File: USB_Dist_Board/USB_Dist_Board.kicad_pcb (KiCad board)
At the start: 2 copper layers, 73 x 64.5 mm, 60 parts, among them P1 CONN_02X06, P2 CONN_01X03, P3 CONN_01X03, P5 CONN_01X04, P6 CONN_01X04, P7 CONN_02X06, Q1 BSS84, Q3 BSS84, SW1 RESET, SW2 BOOT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

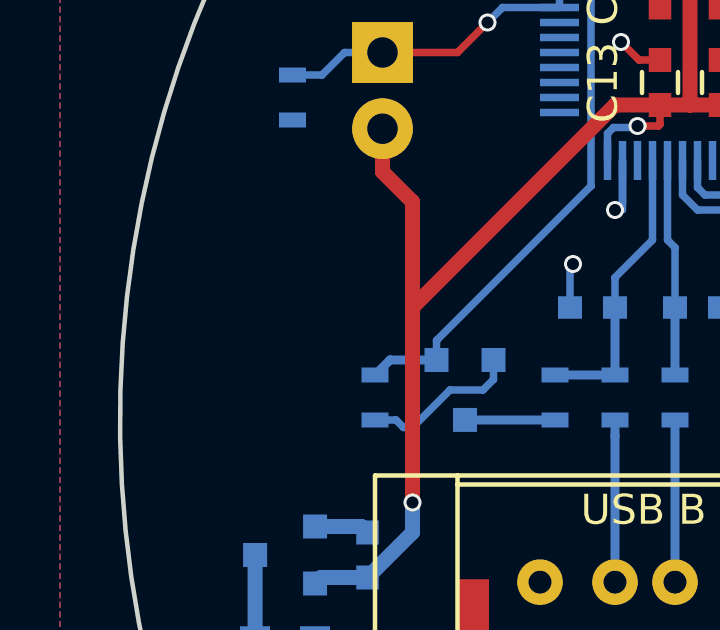
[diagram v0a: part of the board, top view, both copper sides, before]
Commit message: Resize PCBs
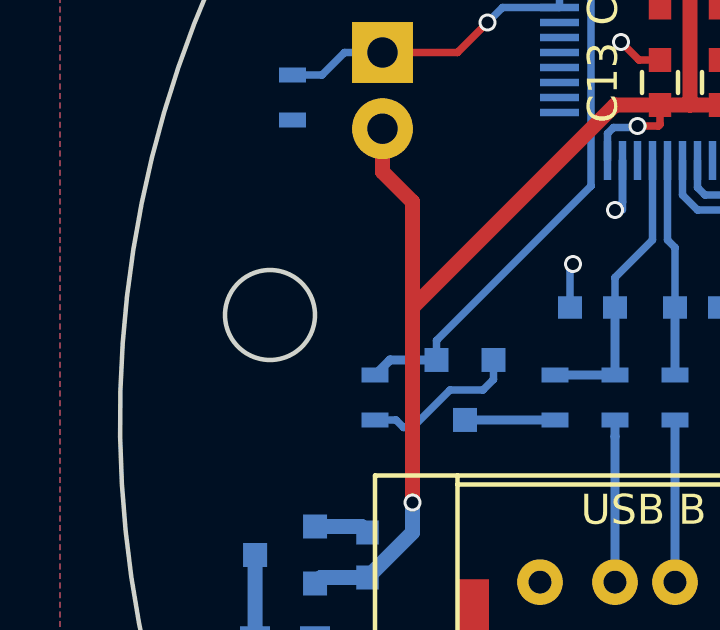
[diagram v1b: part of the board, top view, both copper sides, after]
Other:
- outline, holes or cut-outs redrawn
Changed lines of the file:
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@@
     (area 63.425047 63.425047 136.574953 128.035601)
     (thickness 1.6)
-    (drawings 10)
+    (drawings 11)
     (tracks 451)
     (zones 0)
@@
     )
   )
+  (gr_circle (center 68.5 96.5) (end 68.5 98) (layer Edge.Cuts) (width 0.15))
   (gr_line (start 76.53825 127.9606) (end 123.4617 127.9606) (layer Edge.Cuts) (width 0.15))
   (gr_arc (start 100 100) (end 123.4617 127.9606) (angle -280) (layer Edge.Cuts) (width 0.15))

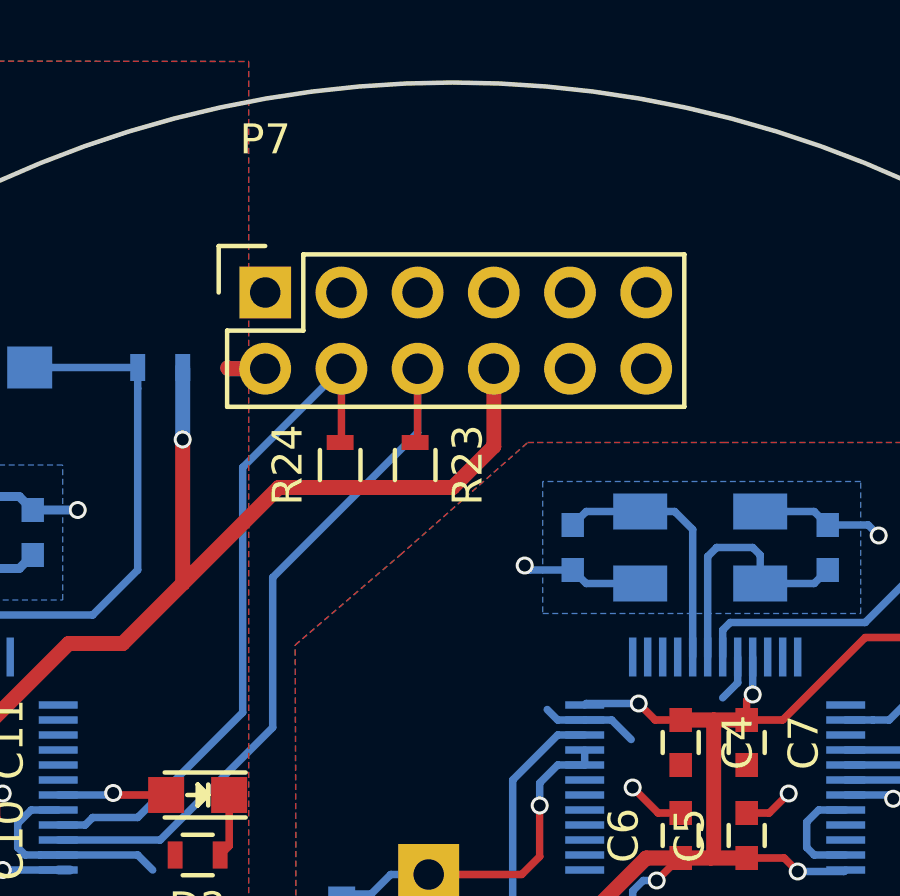
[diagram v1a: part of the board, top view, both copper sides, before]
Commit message: Add Power Distribution Board
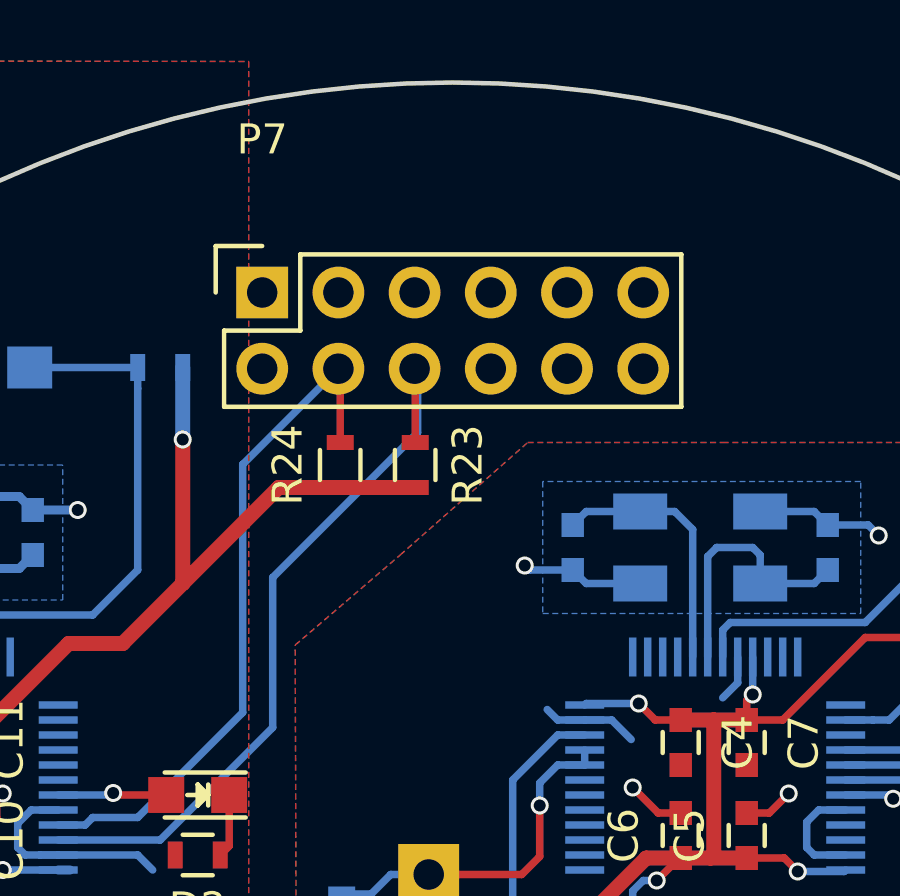
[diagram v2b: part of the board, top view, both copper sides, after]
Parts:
- moved P7 0.10 mm to (93.7, 70.5)
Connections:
- P7 pad 2: /USB_B_GND -> (no net)
- P7 pad 8: /3V3_B -> (no net)
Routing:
- net /3V3_B: track 90.0 -> 84.2 mm
- net /USB_B_GND: track 33.3 -> 30.8 mm
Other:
- net class Default: trace_width 0.25 -> 0.5
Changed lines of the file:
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@@
 (kicad_pcb (version 4) (host pcbnew 4.0.4-stable)
   (general
-    (links 161)
+    (links 159)
     (no_connects 0)
     (area 63.425047 63.425047 136.574953 128.035601)
     (thickness 1.6)
     (drawings 11)
-    (tracks 451)
+    (tracks 445)
     (zones 0)
     (modules 60)
@@
   )
   (setup
-    (last_trace_width 0.25)
+    (last_trace_width 0.5)
     (trace_clearance 0.2)
     (zone_clearance 0.508)
@@
   (net_class Default "This is the default net class."
     (clearance 0.2)
-    (trace_width 0.25)
+    (trace_width 0.5)
     (via_dia 0.6)
     (via_drill 0.4)
@@
   )
   (module Socket_Strips:Socket_Strip_Straight_2x06 (layer F.Cu)
-    (at 93.75 70.5)
+    (at 93.65 70.5)
     (descr "Through hole socket strip")
     (tags "socket strip")
@@
     (fp_line (start -1.55 -1.55) (end -1.55 0) (layer F.SilkS) (width 0.15))
     (pad 1 thru_hole rect (at 0 0) (size 1.7272 1.7272) (drill 1.016) (layers *.Cu *.Mask F.SilkS))
-    (pad 2 thru_hole oval (at 0 2.54) (size 1.7272 1.7272) (drill 1.016) (layers *.Cu *.Mask F.SilkS)
-      (net 50 /USB_B_GND))
+    (pad 2 thru_hole oval (at 0 2.54) (size 1.7272 1.7272) (drill 1.016) (layers *.Cu *.Mask F.SilkS))
     (pad 3 thru_hole oval (at 2.54 0) (size 1.7272 1.7272) (drill 1.016) (layers *.Cu *.Mask F.SilkS))
     (pad 4 thru_hole oval (at 2.54 2.54) (size 1.7272 1.7272) (drill 1.016) (layers *.Cu *.Mask F.SilkS)
@@
       (net 41 /SDA))
     (pad 7 thru_hole oval (at 7.62 0) (size 1.7272 1.7272) (drill 1.016) (layers *.Cu *.Mask F.SilkS))
-    (pad 8 thru_hole oval (at 7.62 2.54) (size 1.7272 1.7272) (drill 1.016) (layers *.Cu *.Mask F.SilkS)
-      (net 39 /3V3_B))
+    (pad 8 thru_hole oval (at 7.62 2.54) (size 1.7272 1.7272) (drill 1.016) (layers *.Cu *.Mask F.SilkS))
     (pad 9 thru_hole oval (at 10.16 0) (size 1.7272 1.7272) (drill 1.016) (layers *.Cu *.Mask F.SilkS))
     (pad 10 thru_hole oval (at 10.16 2.54) (size 1.7272 1.7272) (drill 1.016) (layers *.Cu *.Mask F.SilkS))
@@
   (segment (start 94.2 77) (end 91 80.2) (width 0.5) (layer F.Cu) (net 39))
   (segment (start 98.75 77) (end 96.25 77) (width 0.5) (layer F.Cu) (net 39))
-  (segment (start 101.37 75.63) (end 100 77) (width 0.5) (layer F.Cu) (net 39))
-  (segment (start 100 77) (end 98.75 77) (width 0.5) (layer F.Cu) (net 39))
-  (segment (start 101.37 73.04) (end 101.37 75.63) (width 0.5) (layer F.Cu) (net 39))
   (segment (start 72 100) (end 72.7 100) (width 0.25) (layer B.Cu) (net 39))
   (segment (start 72.7 100) (end 72.95 100.25) (width 0.25) (layer B.Cu) (net 39))
@@
   (via (at 79.75 84.25) (size 0.6) (drill 0.4) (layers F.Cu B.Cu) (net 39))
   (segment (start 86.85 89.75) (end 87.25 89.75) (width 0.3) (layer B.Cu) (net 39))
-  (segment (start 93 84.5) (end 93 76.33) (width 0.25) (layer B.Cu) (net 40))
-  (segment (start 93 76.33) (end 96.29 73.04) (width 0.25) (layer B.Cu) (net 40))
-  (segment (start 89.5 88) (end 93 84.5) (width 0.25) (layer B.Cu) (net 40))
-  (segment (start 88 88) (end 89.5 88) (width 0.25) (layer B.Cu) (net 40))
+  (segment (start 96.25 75.5) (end 96.25 73.1) (width 0.25) (layer F.Cu) (net 40))
+  (segment (start 96.25 73.1) (end 96.19 73.04) (width 0.25) (layer F.Cu) (net 40))
   (segment (start 86.85 88.25) (end 87.75 88.25) (width 0.25) (layer B.Cu) (net 40))
   (segment (start 87.75 88.25) (end 88 88) (width 0.25) (layer B.Cu) (net 40))
-  (segment (start 96.29 73.04) (end 96.29 75.46) (width 0.25) (layer F.Cu) (net 40))
+  (segment (start 88 88) (end 89.5 88) (width 0.25) (layer B.Cu) (net 40))
+  (segment (start 89.5 88) (end 93 84.5) (width 0.25) (layer B.Cu) (net 40))
+  (segment (start 93 84.5) (end 93 76.23) (width 0.25) (layer B.Cu) (net 40))
+  (segment (start 93 76.23) (end 96.19 73.04) (width 0.25) (layer B.Cu) (net 40))
   (segment (start 96.29 75.46) (end 96.25 75.5) (width 0.25) (layer F.Cu) (net 40))
+  (segment (start 98.75 75.5) (end 98.75 73.06) (width 0.25) (layer F.Cu) (net 41))
+  (segment (start 98.75 73.06) (end 98.73 73.04) (width 0.25) (layer F.Cu) (net 41))
   (segment (start 86.85 88.75) (end 90.25 88.75) (width 0.25) (layer B.Cu) (net 41))
   (segment (start 90.25 88.75) (end 94 85) (width 0.25) (layer B.Cu) (net 41))
@@
   (segment (start 94 80) (end 98.83 75.17) (width 0.25) (layer B.Cu) (net 41))
   (segment (start 98.83 75.17) (end 98.83 73.04) (width 0.25) (layer B.Cu) (net 41))
-  (segment (start 98.83 73.04) (end 98.83 75.42) (width 0.25) (layer F.Cu) (net 41))
-  (segment (start 98.83 75.42) (end 98.75 75.5) (width 0.25) (layer F.Cu) (net 41))
   (segment (start 83.8 78.5) (end 84 78.7) (width 0.25) (layer B.Cu) (net 42))
   (segment (start 84 78.7) (end 84 79.7) (width 0.25) (layer B.Cu) (net 42))
@@
   (segment (start 78.1 73) (end 80 73) (width 0.25) (layer B.Cu) (net 50))
   (via (at 80 73) (size 0.6) (drill 0.4) (layers F.Cu B.Cu) (net 50))
-  (segment (start 93.75 73.04) (end 92.528686 73.04) (width 0.5) (layer B.Cu) (net 50))
-  (segment (start 92.528686 73.04) (end 92.5 73.011314) (width 0.5) (layer B.Cu) (net 50))
-  (segment (start 93.75 73.04) (end 92.528686 73.04) (width 0.5) (layer F.Cu) (net 50))
-  (segment (start 92.528686 73.04) (end 92.5 73.011314) (width 0.5) (layer F.Cu) (net 50))
   (segment (start 80.25 91.35) (end 80.25 92.75) (width 0.25) (layer B.Cu) (net 50))
   (segment (start 80.25 92.75) (end 80 93) (width 0.25) (layer B.Cu) (net 50))

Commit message: Commit update
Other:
- outline, holes or cut-outs redrawn
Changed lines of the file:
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@@
     (links 159)
     (no_connects 0)
-    (area 63.425047 63.425047 136.574953 128.035601)
+    (area 61.5 62.75 141.000001 128.035601)
     (thickness 1.6)
     (drawings 11)
@@
     )
   )
-  (gr_circle (center 68.5 96.5) (end 68.5 98) (layer Edge.Cuts) (width 0.15))
+  (gr_circle (center 67 96.5) (end 67 98) (layer Edge.Cuts) (width 0.15))
   (gr_line (start 76.53825 127.9606) (end 123.4617 127.9606) (layer Edge.Cuts) (width 0.15))
   (gr_arc (start 100 100) (end 123.4617 127.9606) (angle -280) (layer Edge.Cuts) (width 0.15))

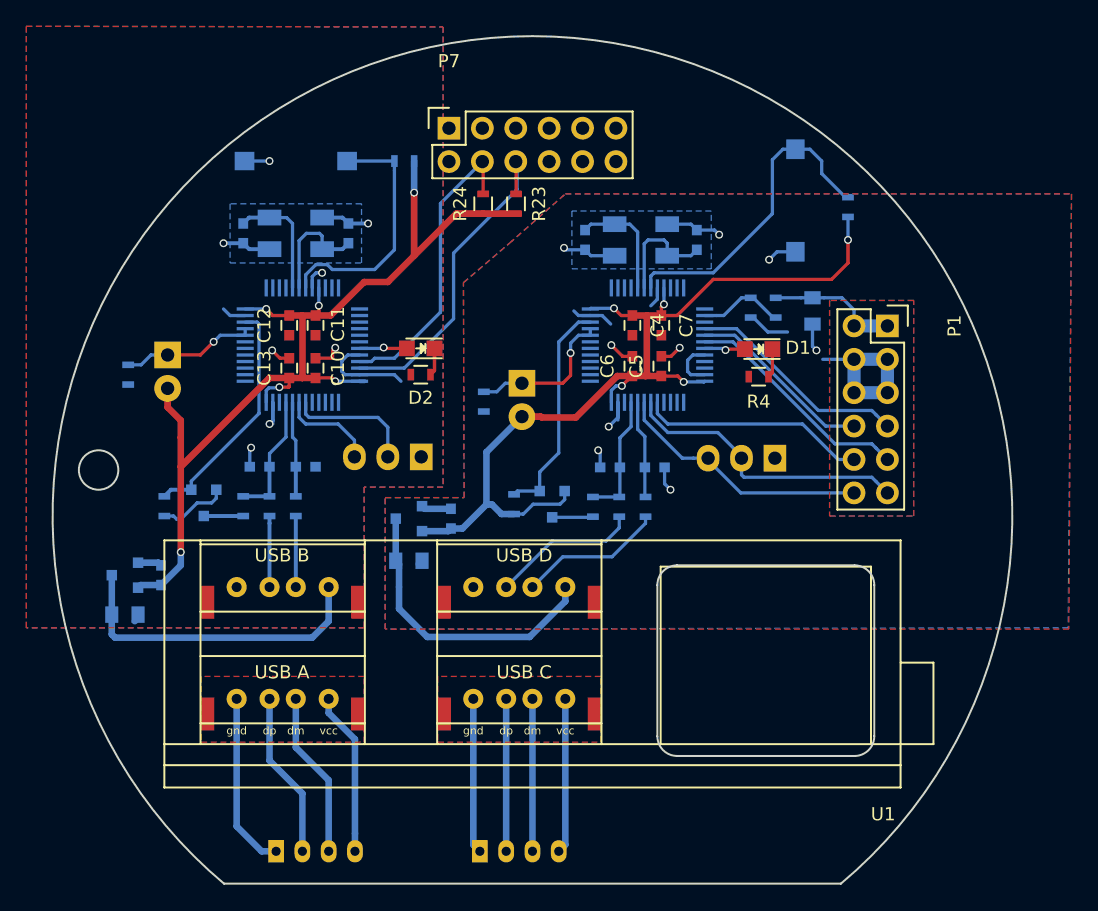
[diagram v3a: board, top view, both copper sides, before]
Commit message: USB_Dist_Board change pin map
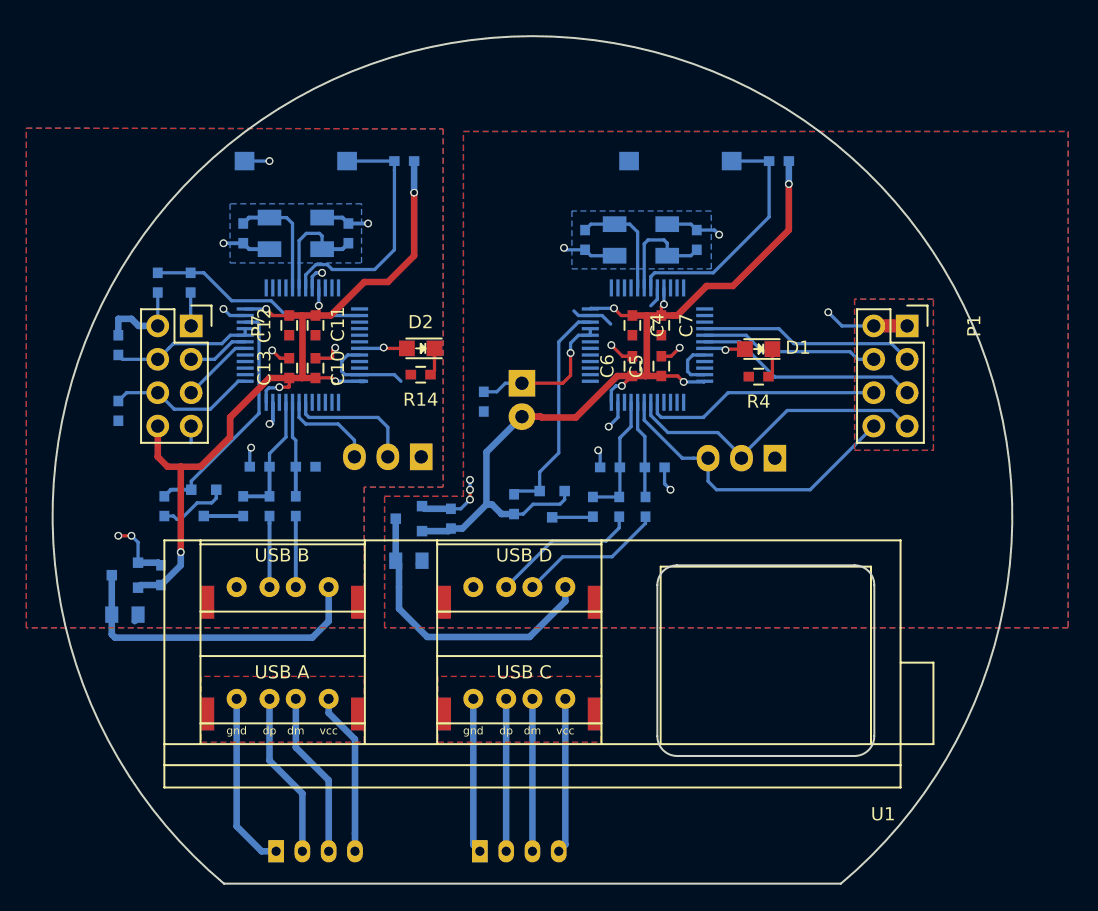
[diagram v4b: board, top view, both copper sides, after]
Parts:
- removed C1: C, Capacitors_SMD:C_0805
- removed R23, R24: R, Resistors_SMD:R_0603
- removed SW4: BOOT, Socket_Strips:Socket_Strip_Straight_1x02
- added R6: R, Capacitors_SMD:C_0603, B.Cu at (68.5, 92.0)
- P1, P7: value CONN_02X06 -> CONN_02X04; footprint Socket_Strips:Socket_Strip_Straight_2x06 -> Socket_Strips:Socket_Strip_Straight_2x04
- R1: value 3.3k -> R; footprint Resistors_SMD:R_0603 -> Capacitors_SMD:C_0603
- R11, R12, R13, R14, R15, R18, R19, R21, R22, R3, R4, R5, R8, R9: footprint Resistors_SMD:R_0603 -> Capacitors_SMD:C_0603
- R2: value 16.7k -> R; footprint Resistors_SMD:R_0603 -> Capacitors_SMD:C_0603
- moved R2 45.1 mm to (71.5, 82.2)
- moved R1 44.5 mm to (74.0, 82.2), turned to 90 degrees
- moved P7 24.7 mm to (74.0, 85.5), turned to 270 degrees
- moved SW1 9.25 mm to (111.2, 73.0), turned to 0 degrees
- moved R9 6.31 mm to (118.8, 73.0), turned to 180 degrees
- moved R18 2.37 mm to (68.5, 87.0), turned to 270 degrees
- moved P1 1.50 mm to (128.5, 85.5)
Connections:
- P1 pad 1: /VCC_Bat -> /USB_D_GND
- P1 pad 2: /VCC_Bat -> /USB_D_GND
- P1 pad 3: /USB_D_GND -> /PWM1
- P1 pad 4: /USB_D_GND -> /PWM2
- P1 pad 5: /USB_D_GND -> /PWM3
- P1 pad 6: /USB_D_GND -> /PWM4
- P1 pad 7: /PWM1 -> /PWM5
- P1 pad 8: /PWM2 -> /PWM6
- P7 pad 1: (no net) -> Net-(P7-Pad1)
- P7 pad 2: (no net) -> /USB_B_GND
- P7 pad 3: (no net) -> /SDA
- P7 pad 4: /SCL -> /BOOT
- P7 pad 5: (no net) -> /SCL
- P7 pad 6: /SDA -> /PWR_SW
- P7 pad 7: (no net) -> /USB_B_GND
- P7 pad 8: (no net) -> /3V3_B
- R1 pad 1: /VCC_Bat -> Net-(P7-Pad1)
- R18 pad 2: /Maple_mini_2/BOOT0 -> /BOOT
- R2 pad 2: /USB_D_GND -> /USB_B_GND
- U2 pad 14: /ADC1 -> (no net)
- U3 pad 14: (no net) -> /ADC1
- U3 pad 21: /SCL -> (no net)
- U3 pad 22: /SDA -> (no net)
- U3 pad 37: (no net) -> /PWR_SW
- U3 pad 42: (no net) -> /SCL
- U3 pad 43: (no net) -> /SDA
- U3 pad 44: /Maple_mini_2/BOOT0 -> /BOOT
- U3 pad 45: /Maple_mini_2/BOOT0 -> /BOOT
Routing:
- net /SDA: track 25.1 -> 4.66 mm
- net /SCL: track 23.0 -> 5.51 mm
- net /USB_D_GND: track 50.0 -> 38.2 mm, vias 9 -> 11
- net /USB_B_GND: track 30.8 -> 42.4 mm, vias 8 -> 11
- net /PWR_SW: track 0.00 -> 11.3 mm
- net /BOOT: track 0.00 -> 11.0 mm
- net /Maple_mini_2/BOOT0: track 10.3 -> 0.00 mm, vias 1 -> 0
- net /3V3_B: track 84.2 -> 74.0 mm
- net /ADC1: track 6.58 -> 16.7 mm
- net /VCC_Bat: track 10.1 -> 0.00 mm
- net Net-(R9-Pad2): track 24.4 -> 18.8 mm
- net /PWM6: track 19.7 -> 24.2 mm
- net Net-(P7-Pad1): track 0.00 -> 2.56 mm
- net /3V3_A: track 71.1 -> 69.4 mm
- net /PWM5: track 22.3 -> 23.9 mm
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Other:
- outline, holes or cut-outs redrawn

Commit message: Main Board & USB Board : Edit EdgeCuts
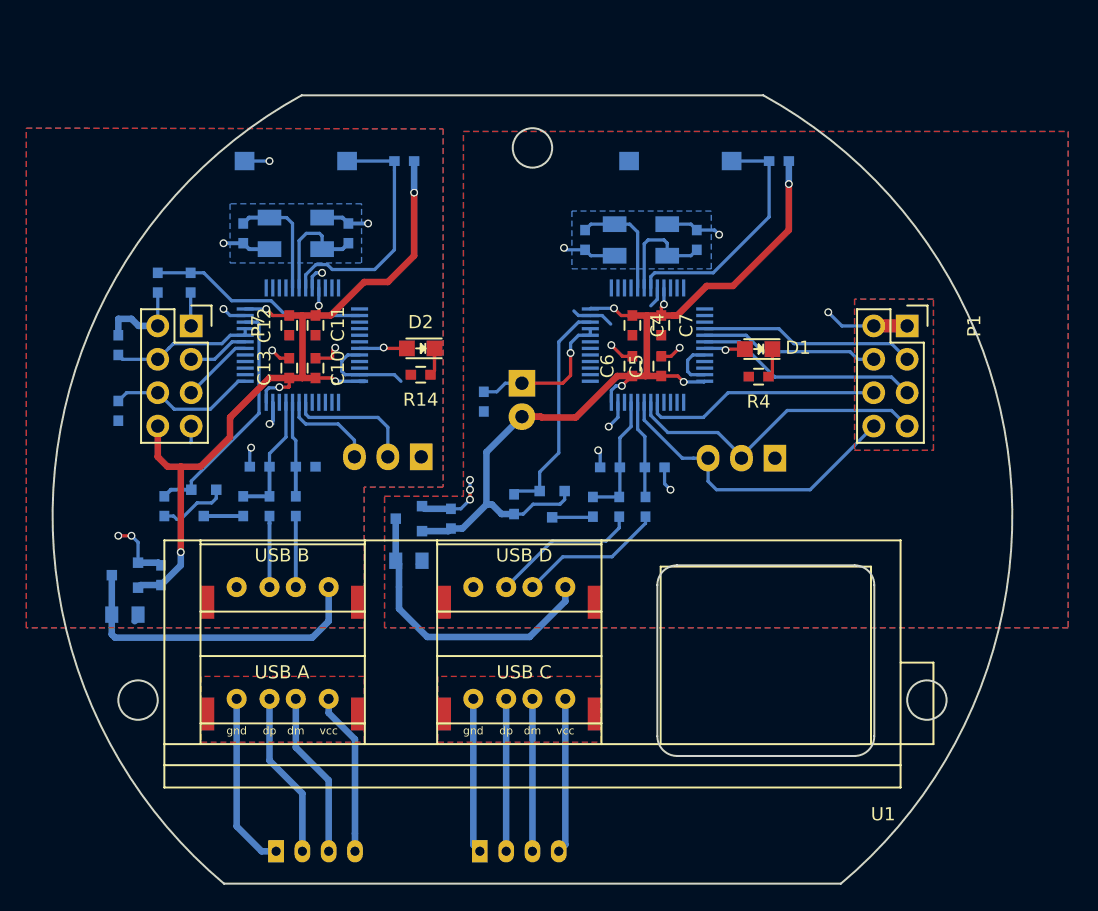
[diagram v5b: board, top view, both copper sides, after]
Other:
- board size 73 x 64.5 mm -> 73 x 60 mm
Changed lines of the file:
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@@
     (links 155)
     (no_connects 0)
-    (area 63.425047 63.425047 136.574953 128.035601)
+    (area 63.424999 67.924999 136.575001 128.035623)
     (thickness 1.6)
-    (drawings 10)
+    (drawings 15)
     (tracks 437)
     (zones 0)
@@
     )
   )
+  (gr_circle (center 100 72) (end 100 73.5) (layer Edge.Cuts) (width 0.15))
+  (gr_circle (center 130 114) (end 130 115.5) (layer Edge.Cuts) (width 0.15))
+  (gr_circle (center 70 114) (end 70 115.5) (layer Edge.Cuts) (width 0.15))
+  (gr_arc (start 100 100) (end 82.44295 68) (angle -111.2482815) (layer Edge.Cuts) (width 0.15))
+  (gr_line (start 82.44295 68) (end 117.55705 68) (layer Edge.Cuts) (width 0.15))
   (gr_line (start 76.53825 127.9606) (end 123.4617 127.9606) (layer Edge.Cuts) (width 0.15))
-  (gr_arc (start 100 100) (end 123.4617 127.9606) (angle -280) (layer Edge.Cuts) (width 0.15))
+  (gr_arc (start 100 100) (end 117.55705 68) (angle 111.2482815) (layer Edge.Cuts) (width 0.15))
   (gr_line (start 111 118.25) (end 124.5 118.25) (layer Edge.Cuts) (width 0.15))
   (gr_line (start 126 105.25) (end 126 116.75) (layer Edge.Cuts) (width 0.15))
